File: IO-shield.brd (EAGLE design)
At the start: 68.6 x 53.3 mm, 36 parts, among them J2 8x1F-H8.5, J3 8x1F-H8.5, J4 6x1F-H8.5

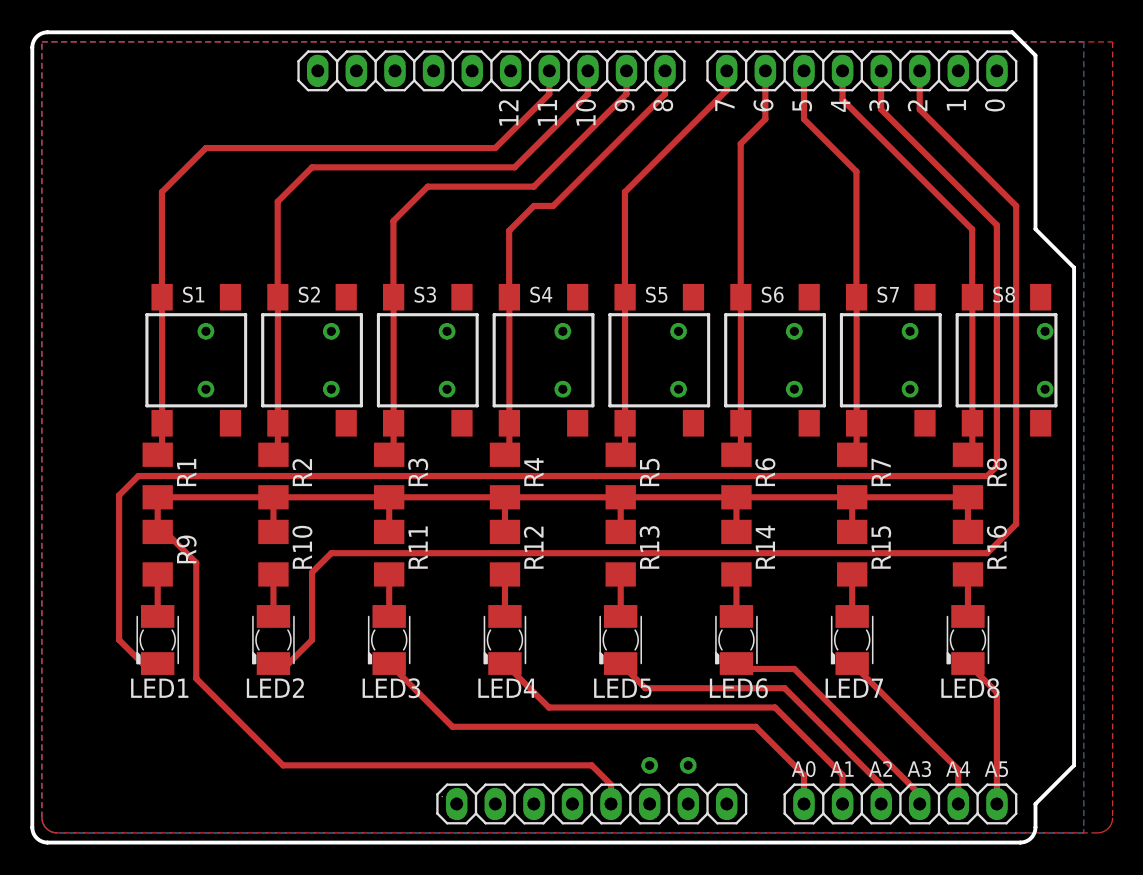
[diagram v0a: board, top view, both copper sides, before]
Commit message: extended shield with jumpers, added part list and picture
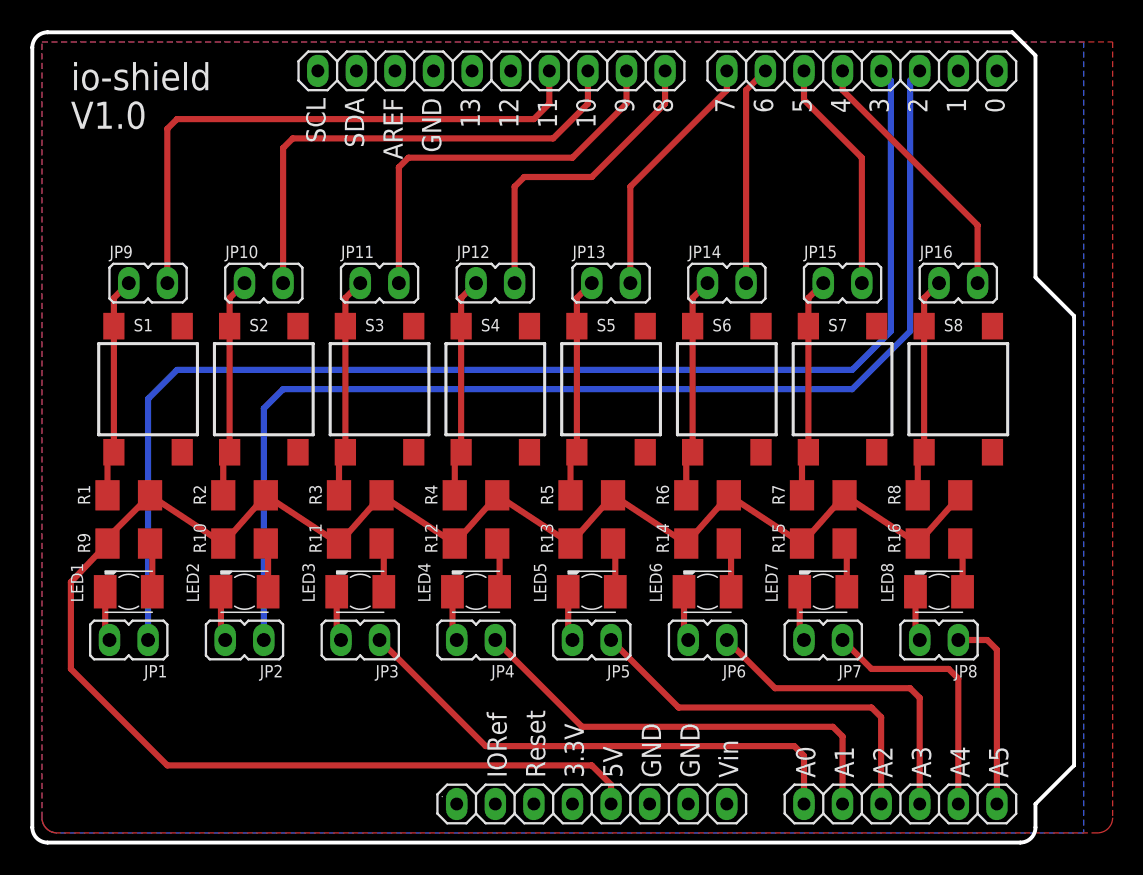
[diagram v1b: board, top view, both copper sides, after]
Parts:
- added J1: 10x1F-H8.5, SmartPrj:1X10
- added JP10, JP11, JP12, JP13, JP14, JP15, JP16, JP2, JP3, JP4, JP5, JP6, JP7, JP8, JP9: (no value), jumper:JP1
- JP1: value 10x1F-H8.5 -> (none); device SmartPrj:1X10 -> jumper:JP1
- moved JP1 44.4 mm to (6.35, 13.3), turned to 90 degrees
- moved S6 3.70 mm to (45.7, 29.8)
- moved S8 3.70 mm to (61.0, 29.8)
- moved LED1 3.70 mm to (6.35, 16.5), turned to 180 degrees
- moved LED3 3.70 mm to (21.6, 16.5), turned to 180 degrees
- moved LED5 3.70 mm to (36.8, 16.5), turned to 180 degrees
- moved LED7 3.70 mm to (52.1, 16.5), turned to 180 degrees
- moved LED8 3.70 mm to (59.7, 16.5), turned to 180 degrees
- moved S3 3.70 mm to (22.9, 29.8)
- moved S4 3.70 mm to (30.5, 29.8)
- moved S1 3.70 mm to (7.62, 29.8)
- moved LED2 3.70 mm to (14.0, 16.5), turned to 180 degrees
- moved S2 3.70 mm to (15.2, 29.8)
- moved LED4 3.70 mm to (29.2, 16.5), turned to 180 degrees
- moved LED6 3.70 mm to (44.5, 16.5), turned to 180 degrees
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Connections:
- new net N$1: JP1.2, LED1.C
- new net N$17: JP15.1, R7.1, S7.3, S7.4
- new net N$18: JP16.1, R8.1, S8.3, S8.4
- new net N$19: JP3.2, LED3.C
- new net N$2: JP2.2, LED2.C
- new net N$20: JP4.2, LED4.C
- new net N$21: JP5.2, LED5.C
- new net N$22: JP6.2, LED6.C
- new net N$23: JP7.2, LED7.C
- new net N$24: JP8.2, LED8.C
- new net N$3: JP9.1, R1.1, S1.3, S1.4
- new net N$4: JP10.1, R2.1, S2.3, S2.4
- new net N$5: JP11.1, R3.1, S3.3, S3.4
- new net N$6: JP12.1, R4.1, S4.3, S4.4
- new net N$7: JP13.1, R5.1, S5.3, S5.4
- new net N$8: JP14.1, R6.1, S6.3, S6.4
- net GND: now also J1.7; no longer JP1.7
- net I1: now also J1.4, JP9.2; no longer JP1.4, R1.1, S1.3, S1.4
- net I2: now also J1.3, JP10.2; no longer JP1.3, R2.1, S2.3, S2.4
- net I3: now also J1.2, JP11.2; no longer JP1.2, R3.1, S3.3, S3.4
- net I4: now also J1.1, JP12.2; no longer JP1.1, R4.1, S4.3, S4.4
- net I5: now also JP13.2; no longer R5.1, S5.3, S5.4
- net I6: now also JP14.2; no longer R6.1, S6.3, S6.4
- net I7: now also JP15.2; no longer R7.1, S7.3, S7.4
- net I8: now also JP16.2; no longer R8.1, S8.3, S8.4
- net Q1: now also JP1.1; no longer LED1.C
- net Q2: now also JP2.1; no longer LED2.C
- net Q3: now also JP3.1; no longer LED3.C
- net Q4: now also JP4.1; no longer LED4.C
- net Q5: now also JP5.1; no longer LED5.C
- net Q6: now also JP6.1; no longer LED6.C
- net Q7: now also JP7.1; no longer LED7.C
- net Q8: now also JP8.1; no longer LED8.C
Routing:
- net Q1: track 100.5 -> 84.0 mm
- net N$8: track 0.00 -> 14.5 mm
- net N$6: track 0.00 -> 14.5 mm
- net N$4: track 0.00 -> 14.5 mm
- net N$3: track 0.00 -> 14.5 mm
- net N$7: track 0.00 -> 14.5 mm
- net N$5: track 0.00 -> 14.5 mm
- net N$18: track 0.00 -> 14.5 mm
- net N$17: track 0.00 -> 14.5 mm
- net I6: track 26.2 -> 14.5 mm
- net I5: track 28.3 -> 16.6 mm
- net I7: track 27.0 -> 15.5 mm
- net I8: track 29.1 -> 17.7 mm
- net Q2: track 87.8 -> 77.3 mm
- net I4: track 30.6 -> 20.7 mm
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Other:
- outline, holes or cut-outs redrawn
- board text added: "13"
- board text added: "3.3V"
- board text added: "5V"
- board text added: "AREF"
- board text added: "GND"
- board text added: "IORef"
- board text added: "Reset"
- board text added: "V1.0"
- board text added: "Vin"
- board text added: "io-shield"

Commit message: changed position of the jumpers
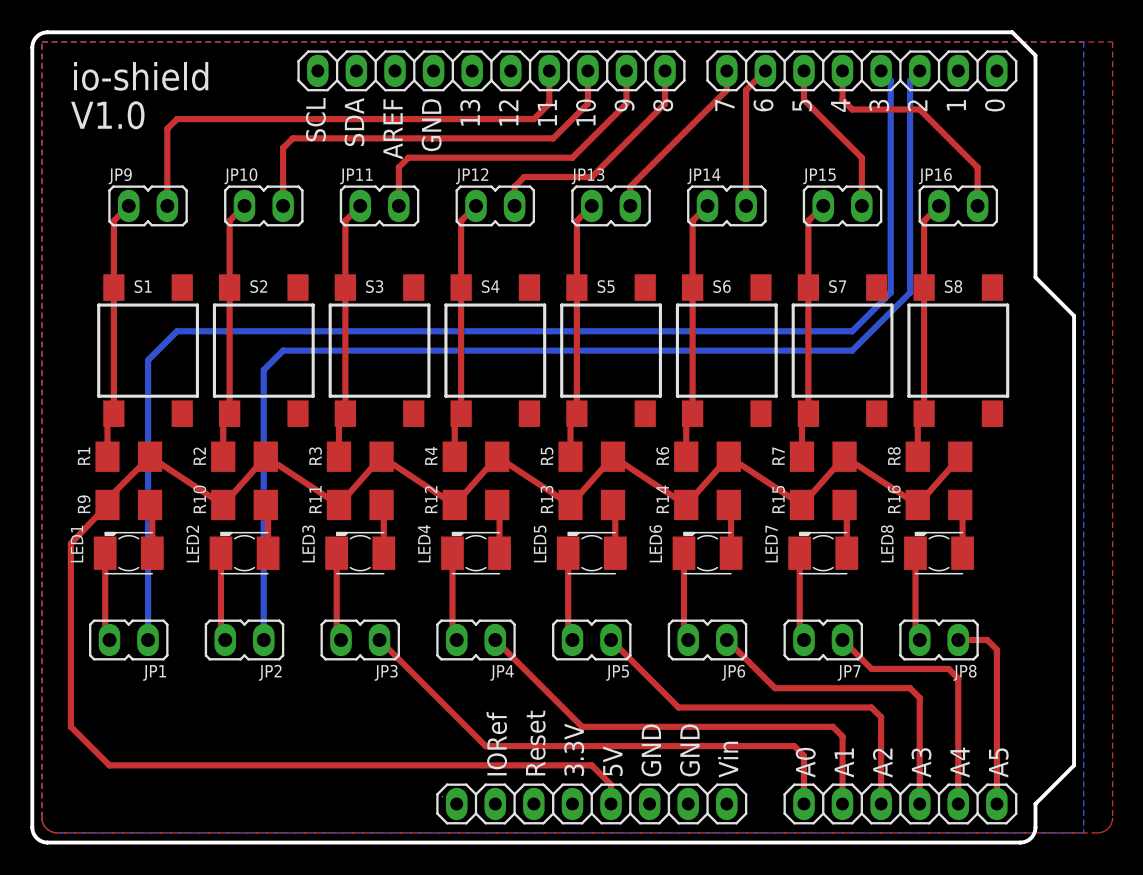
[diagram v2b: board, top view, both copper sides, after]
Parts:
- moved JP10 5.08 mm to (15.2, 41.9)
- moved JP11 5.08 mm to (22.9, 41.9)
- moved JP12 5.08 mm to (30.5, 41.9)
- moved JP13 5.08 mm to (38.1, 41.9)
- moved JP14 5.08 mm to (45.7, 41.9)
- moved JP15 5.08 mm to (53.3, 41.9)
- moved JP16 5.08 mm to (61.0, 41.9)
- moved JP9 5.08 mm to (7.62, 41.9)
- moved R10 2.54 mm to (14.0, 22.2)
- moved R11 2.54 mm to (21.6, 22.2)
- moved R12 2.54 mm to (29.2, 22.2)
- moved R13 2.54 mm to (36.8, 22.2)
- moved R14 2.54 mm to (44.5, 22.2)
- moved R15 2.54 mm to (52.1, 22.2)
- moved R16 2.54 mm to (59.7, 22.2)
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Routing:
- net I2: track 32.3 -> 27.2 mm
- net I7: track 15.5 -> 10.5 mm
- net I6: track 14.5 -> 9.42 mm
- net I4: track 20.7 -> 15.6 mm
- net I3: track 26.5 -> 21.4 mm
- net I1: track 38.1 -> 33.1 mm
- net I5: track 16.6 -> 11.5 mm
- net VCC: track 123.6 -> 128.3 mm
- net N$6: track 14.5 -> 17.1 mm
- net N$7: track 14.5 -> 17.1 mm
- net N$5: track 14.5 -> 17.1 mm
- net N$18: track 14.5 -> 17.1 mm
- net N$17: track 14.5 -> 17.1 mm
- net N$8: track 14.5 -> 17.1 mm
- net N$4: track 14.5 -> 17.1 mm
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
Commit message: added 2 potis and header
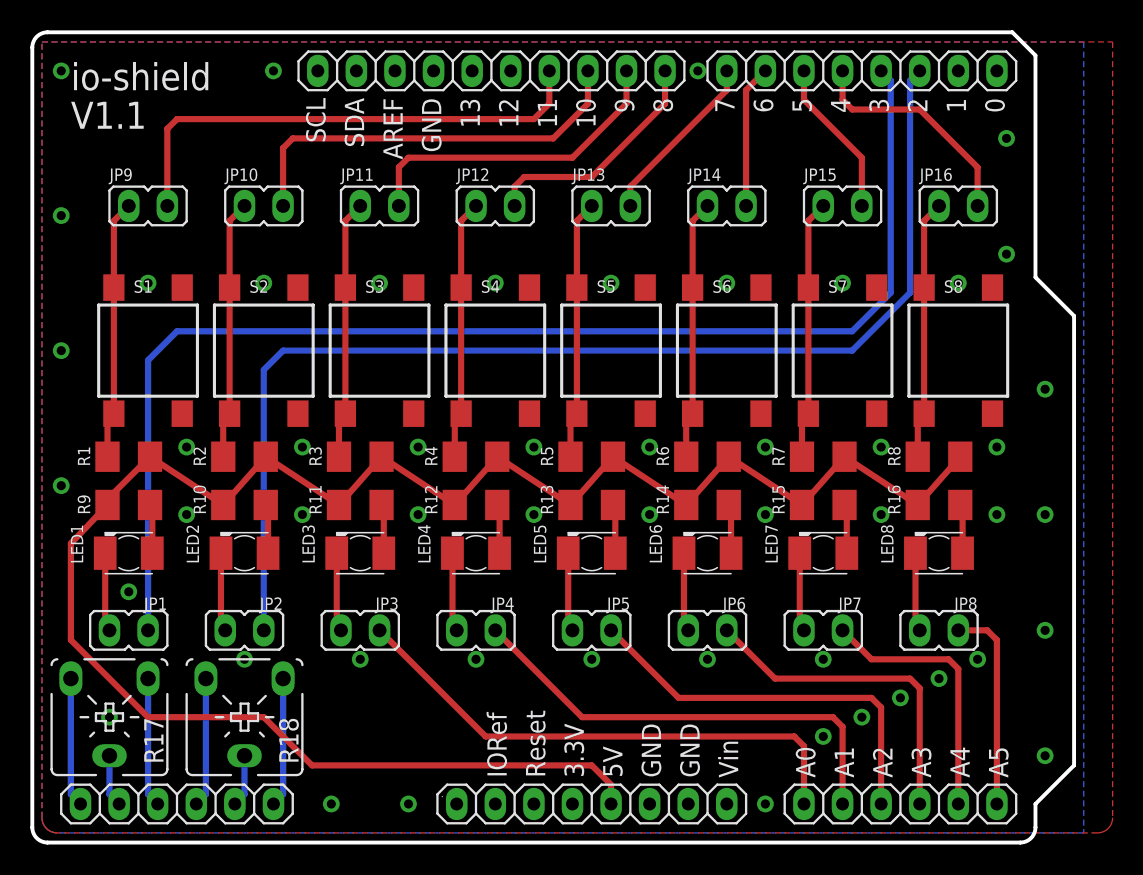
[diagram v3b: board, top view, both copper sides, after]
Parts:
- added J5: 6x1F-H8.5, SmartPrj:1X06
- added R17, R18: (no value), pot:CA6V
- moved JP1 0.63 mm to (6.35, 14.0)
- moved JP2 0.63 mm to (14.0, 14.0)
- moved JP3 0.63 mm to (21.6, 14.0)
- moved JP4 0.63 mm to (29.2, 14.0)
- moved JP5 0.63 mm to (36.8, 14.0)
- moved JP6 0.63 mm to (44.5, 14.0)
- moved JP7 0.63 mm to (52.1, 14.0)
- moved JP8 0.63 mm to (59.7, 14.0)
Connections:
- new net N$25: J5.2, R17.S
- new net N$26: J5.1, R17.E
- new net N$27: J5.3, R17.A
- new net N$28: J5.5, R18.S
- new net N$29: J5.4, R18.E
- new net N$30: J5.6, R18.A
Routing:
- net N$30: track 0.00 -> 8.52 mm
- net N$29: track 0.00 -> 8.52 mm
- net N$27: track 0.00 -> 8.52 mm
- net N$26: track 0.00 -> 8.52 mm
- net N$28: track 0.00 -> 3.44 mm
- net N$25: track 0.00 -> 3.44 mm
- net VCC: track 128.3 -> 125.0 mm
- net Q2: track 77.3 -> 76.7 mm
- net Q7: track 16.9 -> 17.6 mm
- net Q8: track 13.0 -> 13.6 mm
- net N$24: track 5.83 -> 5.20 mm
- net N$23: track 5.83 -> 5.20 mm
- net N$22: track 5.83 -> 5.20 mm
- net N$21: track 5.83 -> 5.20 mm
- net N$20: track 5.83 -> 5.20 mm
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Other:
- board text added: "V1.1"
- board text removed: "V1.0"
